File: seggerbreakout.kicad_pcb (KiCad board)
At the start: 2 copper layers, 29.5 x 28 mm, 3 parts, among them P1 SWD, P2 JTAG, P3 JTAG

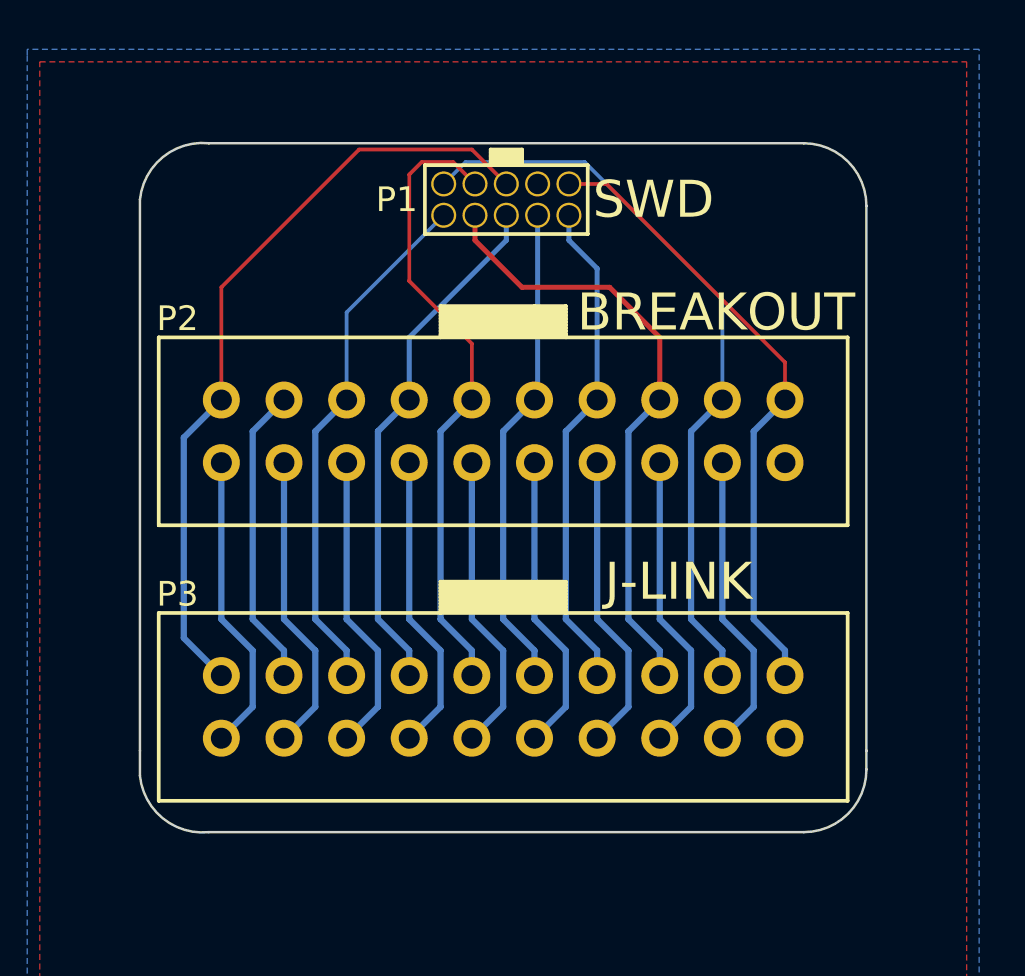
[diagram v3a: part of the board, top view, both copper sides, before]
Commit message: Hole resize and rerouting
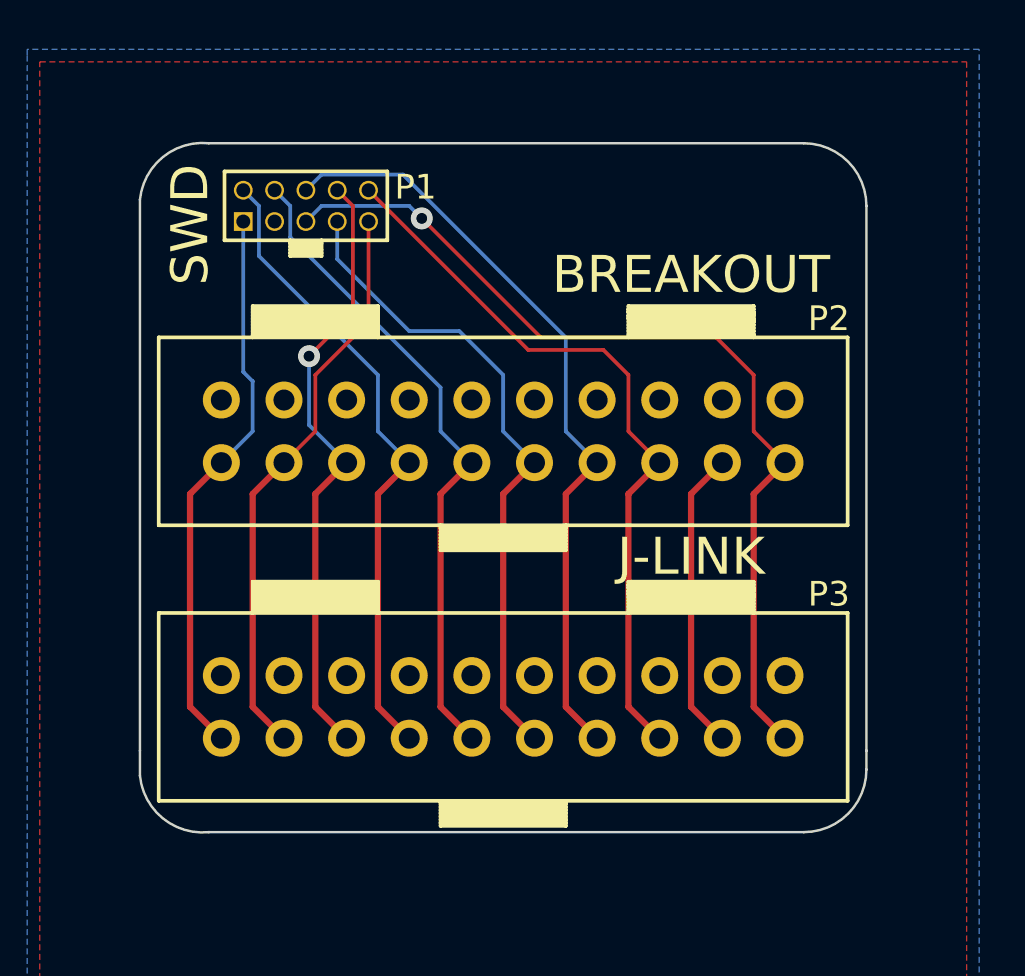
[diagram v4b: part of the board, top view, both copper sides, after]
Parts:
- moved P1 9.40 mm to (189.7, 120.9), turned to 180 degrees
- moved P2 2.54 mm to (198.4, 131.3), turned to 0 degrees
- moved P3 2.54 mm to (198.4, 142.5), turned to 0 degrees
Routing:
- net GND: track 110.1 -> 0.00 mm
- net /TDO: track 21.4 -> 31.4 mm
- net /RESET: track 21.4 -> 30.0 mm
- net /nTRST: track 30.3 -> 23.4 mm
- net /TCK: track 19.8 -> 26.6 mm
- net /5V: track 31.5 -> 37.6 mm, vias 0 -> 1
- net /TMS: track 20.2 -> 26.1 mm
- net /VTref: track 25.5 -> 22.7 mm
- net /RTCK: track 25.7 -> 26.5 mm
- net /TDI: vias 0 -> 1

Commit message: Sent to fab
Vendor: OSHPark, LLC
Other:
- board text added: "J-LINK Breakout+SWD 2014-08-31 open.konspyre.org/jswd"
- board text removed: "J-LINK Breakout+SWD 2014-08-18 open.konspyre.org/jswd"
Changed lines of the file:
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@@
     (area 179.07 114.554 217.678001 153.162001)
     (thickness 1.6)
-    (drawings 74)
+    (drawings 71)
     (tracks 79)
     (zones 0)
@@
   (page A3)
   (layers
-    (15 F.Cu signal)
-    (0 B.Cu signal)
+    (15 F.Cu signal hide)
+    (0 B.Cu signal hide)
     (16 B.Adhes user)
     (17 F.Adhes user)
@@
   (module JTAG_SMALL (layer F.Cu)
     (at 189.738 120.904 180)
-    (fp_text reference P1 (at -5.08 0.762 180) (layer F.SilkS)
+    (fp_text reference P1 (at 3.81 0 180) (layer F.SilkS)
       (effects (font (size 1 1) (thickness 0.15)))
     )
@@
     )
   )
+  (gr_line (start 196.85 126.238) (end 196.85 125.984) (angle 90) (layer B.SilkS) (width 0.2))
+  (gr_line (start 192.024 126.746) (end 192.024 127.762) (angle 90) (layer B.SilkS) (width 0.2))
+  (gr_line (start 189.484 127.508) (end 189.484 127.762) (angle 90) (layer B.SilkS) (width 0.2))
   (gr_line (start 188.214 133.35) (end 188.214 133.604) (angle 90) (layer B.SilkS) (width 0.2))
   (gr_line (start 207.264 132.588) (end 207.264 133.35) (angle 90) (layer B.SilkS) (width 0.2))
@@
   (gr_line (start 186.944 133.35) (end 189.484 133.35) (angle 90) (layer B.SilkS) (width 0.2))
   (gr_line (start 186.944 132.588) (end 186.944 133.35) (angle 90) (layer B.SilkS) (width 0.2))
-  (gr_text "J-LINK Breakout+SWD\n2014-08-18\nopen.konspyre.org/jswd" (at 202.438 134.62) (layer B.SilkS)
+  (gr_text "J-LINK Breakout+SWD\n2014-08-31\nopen.konspyre.org/jswd" (at 202.438 134.62) (layer B.SilkS)
     (effects (font (size 1.0668 1.0668) (thickness 0.2667)) (justify mirror))
   )
-  (gr_text BREAKOUT (at 205.994 123.698) (layer F.SilkS)
-    (effects (font (size 1.5 1.5) (thickness 0.3)))
-  )
-  (gr_text J-LINK (at 205.994 135.128) (layer F.SilkS)
-    (effects (font (size 1.5 1.5) (thickness 0.3)))
-  )
-  (gr_text SWD (at 185.674 121.666 90) (layer F.SilkS)
-    (effects (font (size 1.5 1.5) (thickness 0.3)))
+  (gr_text BREAKOUT (at 198.374 125.349) (layer F.SilkS)
+    (effects (font (size 1.016 1.016) (thickness 0.254)))
+  )
+  (gr_text J-LINK (at 198.374 136.525) (layer F.SilkS)
+    (effects (font (size 1.016 1.016) (thickness 0.254)))
+  )
+  (gr_text SWD (at 198.374 120.904) (layer F.SilkS)
+    (effects (font (size 1.016 1.016) (thickness 0.254)))
   )
   (gr_text GND (at 188.214 134.874) (layer B.SilkS)
@@
   )
   (gr_line (start 199.39 125.476) (end 199.39 124.968) (angle 90) (layer B.SilkS) (width 0.2))
-  (gr_line (start 201.676 125.476) (end 201.676 124.968) (angle 90) (layer B.SilkS) (width 0.2))
-  (gr_line (start 196.85 126.238) (end 196.85 125.73) (angle 90) (layer B.SilkS) (width 0.2))
-  (gr_line (start 192.024 127) (end 192.024 126.492) (angle 90) (layer B.SilkS) (width 0.2))
   (gr_line (start 186.944 127.508) (end 186.944 127.762) (angle 90) (layer B.SilkS) (width 0.2))
   (gr_line (start 209.804 127.508) (end 209.804 127.762) (angle 90) (layer B.SilkS) (width 0.2))
@@
   (gr_line (start 197.104 127.508) (end 197.104 127.762) (angle 90) (layer B.SilkS) (width 0.2))
   (gr_line (start 194.564 127.508) (end 194.564 127.762) (angle 90) (layer B.SilkS) (width 0.2))
-  (gr_line (start 192.024 127.508) (end 192.024 127.762) (angle 90) (layer B.SilkS) (width 0.2))
-  (gr_line (start 189.484 127.254) (end 189.484 127.762) (angle 90) (layer B.SilkS) (width 0.2))
-  (gr_line (start 192.024 127) (end 192.024 127.508) (angle 90) (layer B.SilkS) (width 0.2))
   (gr_line (start 194.564 125.476) (end 194.564 127.508) (angle 90) (layer B.SilkS) (width 0.2))
   (gr_line (start 197.104 126.492) (end 197.104 127.508) (angle 90) (layer B.SilkS) (width 0.2))
@@
   (gr_line (start 209.042 126.492) (end 209.804 127.254) (angle 90) (layer B.SilkS) (width 0.2))
   (gr_line (start 186.944 124.46) (end 186.944 127.508) (angle 90) (layer B.SilkS) (width 0.2))
-  (gr_text "5V\nDBGRQ\nRESET\nTDO\nRTCK\nTCK\nTMS\nTDI\nnTRST\nVTref" (at 187.452 121.92 90) (layer B.SilkS)
+  (gr_text "5V\nDBGRQ\nRESET\nTDO\nRTCK\nTCK\nTMS\nTDI\nnTRST\nVTref" (at 187.452 122.174 90) (layer B.SilkS)
     (effects (font (size 1.524 1.016) (thickness 0.254)) (justify left mirror))
   )

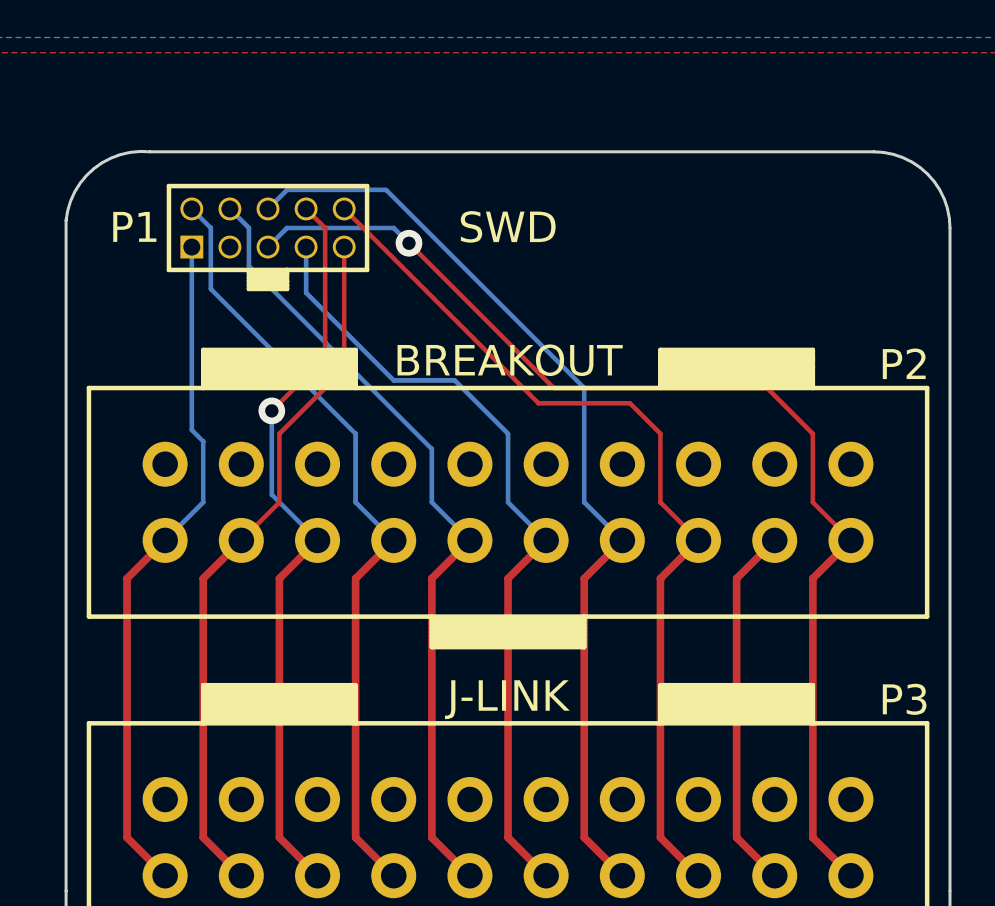
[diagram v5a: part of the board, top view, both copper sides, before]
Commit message: Multiple fixes from last fabbed revision
1. Enlarged annular rings on SWD breakout and made them square, for better solderability

2. On the last revision, I flipped the large pin headers for ease of use with the SWD connector cable,
however I neglected to also flip the silkscreen indicators as well. This has been fixed.

3. Corrected the silkscreen for the large pin headers, they were a bit larger than the actual keyed tabs.

Parts:

20P header: D2520-6002-AR - Vendor: Mouser
SWD header (open, non-keyed): 952-1383-ND - Vendor: Digikey
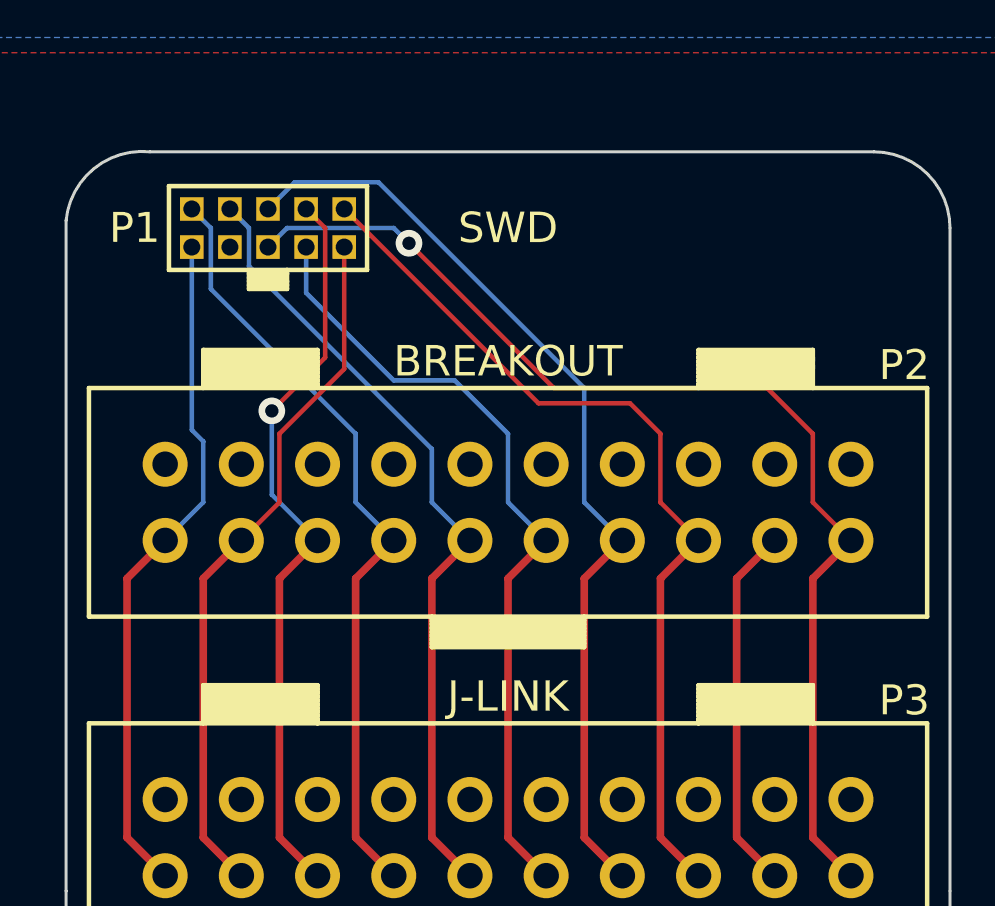
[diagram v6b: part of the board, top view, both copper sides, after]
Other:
- board text added: "2014-08-31"
- board text added: "J-LINK Breakout+SWD"
- board text added: "open.konspyre.org/jswd"
- board text removed: "J-LINK Breakout+SWD 2014-08-31 open.konspyre.org/jswd"
